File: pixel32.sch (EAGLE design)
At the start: 77 parts, among them CON1 B7B-PH-K-S-SIDE, CON10 PINHEAD_1X01-2.54, CON11 PINHEAD_1X01-2.54, CON12 PINHEAD_1X02-2.54, CON13 PINHEAD_1X07-2, CON14 PINHEAD_1X07-2, CON2 B7B-PH-K-S-SIDE, CON3 PINHEAD_1X02-2.54, CON4 PINHEAD_1X01-2.54, CON5 PINHEAD_1X01-2.54, CON6 PINHEAD_1X01-2.54, CON7 PINHEAD_1X01-2.54, CON8 PINHEAD_1X01-2.54, CON9 PINHEAD_1X01-2.54, IC1 STM32F030K6TX-LQFP32(7X7), IC3 ST3485SOIC8, IC6 MC74VHC1GT125, IC7 MC74VHC1GT125, IC8 LM317, Y1 16MHz

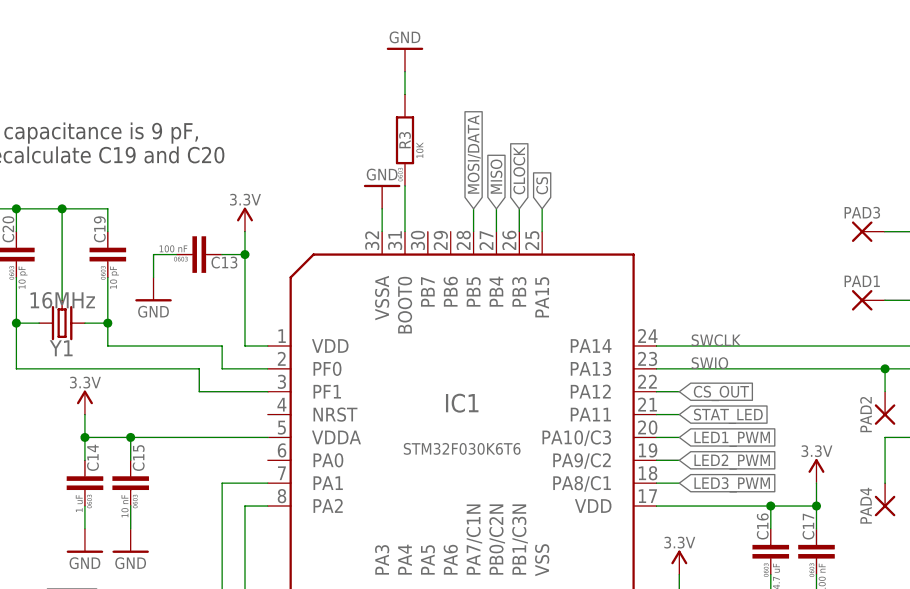
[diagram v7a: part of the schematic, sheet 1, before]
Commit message: added reset pad
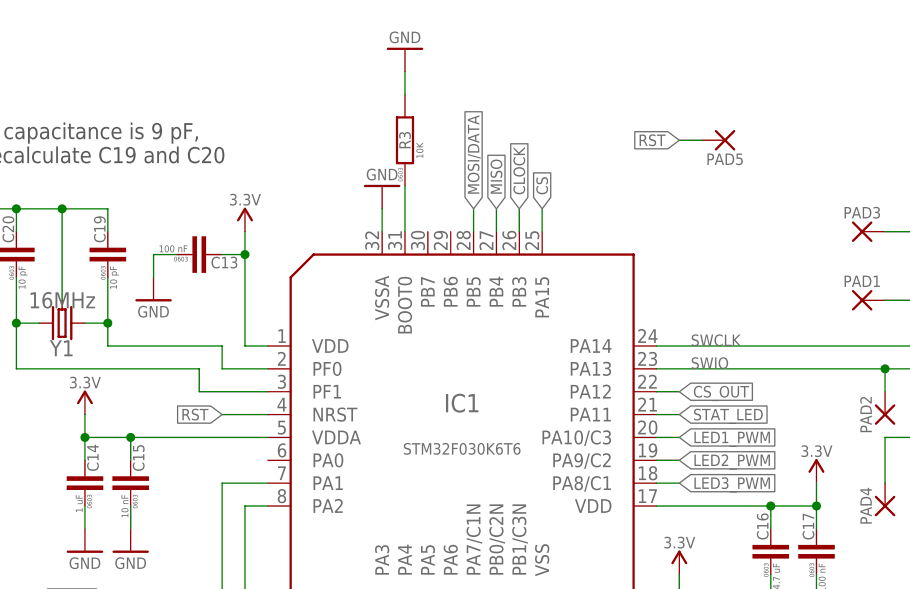
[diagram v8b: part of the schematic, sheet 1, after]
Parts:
- added PAD5: WIREPADSMD2.5-1.8, wirepad:WIREPADSMD2.5-1.8
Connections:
- new net RST: IC1.NRST, PAD5.P
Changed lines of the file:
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@@
 <grid distance="0.1" unitdist="inch" unit="inch" style="lines" multiple="1" display="no" altdistance="0.01" altunitdist="inch" altunit="inch"/>
 <layers>
-<layer number="1" name="Top" color="4" fill="1" visible="yes" active="no"/>
-<layer number="2" name="Route2" color="1" fill="3" visible="yes" active="no"/>
-<layer number="3" name="Route3" color="4" fill="3" visible="yes" active="no"/>
-<layer number="4" name="Route4" color="1" fill="4" visible="yes" active="no"/>
-<layer number="5" name="Route5" color="4" fill="4" visible="yes" active="no"/>
-<layer number="6" name="Route6" color="1" fill="8" visible="yes" active="no"/>
-<layer number="7" name="Route7" color="4" fill="8" visible="yes" active="no"/>
-<layer number="8" name="Route8" color="1" fill="2" visible="yes" active="no"/>
-<layer number="9" name="Route9" color="4" fill="2" visible="yes" active="no"/>
-<layer number="10" name="Route10" color="1" fill="7" visible="yes" active="no"/>
-<layer number="11" name="Route11" color="4" fill="7" visible="yes" active="no"/>
-<layer number="12" name="Route12" color="1" fill="5" visible="yes" active="no"/>
-<layer number="13" name="Route13" color="4" fill="5" visible="yes" active="no"/>
-<layer number="14" name="Route14" color="1" fill="6" visible="yes" active="no"/>
-<layer number="15" name="Route15" color="4" fill="6" visible="yes" active="no"/>
-<layer number="16" name="Bottom" color="1" fill="1" visible="yes" active="no"/>
-<layer number="17" name="Pads" color="2" fill="1" visible="yes" active="no"/>
-<layer number="18" name="Vias" color="2" fill="1" visible="yes" active="no"/>
-<layer number="19" name="Unrouted" color="6" fill="1" visible="yes" active="no"/>
-<layer number="20" name="Dimension" color="15" fill="1" visible="yes" active="no"/>
-<layer number="21" name="tPlace" color="7" fill="1" visible="yes" active="no"/>
-<layer number="22" name="bPlace" color="7" fill="1" visible="yes" active="no"/>
-<layer number="23" name="tOrigins" color="15" fill="1" visible="yes" active="no"/>
-<layer number="24" name="bOrigins" color="15" fill="1" visible="yes" active="no"/>
-<layer number="25" name="tNames" color="7" fill="1" visible="yes" active="no"/>
-<layer number="26" name="bNames" color="7" fill="1" visible="yes" active="no"/>
-<layer number="27" name="tValues" color="7" fill="1" visible="yes" active="no"/>
-<layer number="28" name="bValues" color="7" fill="1" visible="yes" active="no"/>
+<layer number="1" name="Top" color="4" fill="1" visible="no" active="no"/>
+<layer number="2" name="Route2" color="1" fill="3" visible="no" active="no"/>
+<layer number="3" name="Route3" color="4" fill="3" visible="no" active="no"/>
+<layer number="4" name="Route4" color="1" fill="4" visible="no" active="no"/>
+<layer number="5" name="Route5" color="4" fill="4" visible="no" active="no"/>
+<layer number="6" name="Route6" color="1" fill="8" visible="no" active="no"/>
+<layer number="7" name="Route7" color="4" fill="8" visible="no" active="no"/>
+<layer number="8" name="Route8" color="1" fill="2" visible="no" active="no"/>
+<layer number="9" name="Route9" color="4" fill="2" visible="no" active="no"/>
+<layer number="10" name="Route10" color="1" fill="7" visible="no" active="no"/>
+<layer number="11" name="Route11" color="4" fill="7" visible="no" active="no"/>
+<layer number="12" name="Route12" color="1" fill="5" visible="no" active="no"/>
+<layer number="13" name="Route13" color="4" fill="5" visible="no" active="no"/>
+<layer number="14" name="Route14" color="1" fill="6" visible="no" active="no"/>
+<layer number="15" name="Route15" color="4" fill="6" visible="no" active="no"/>
+<layer number="16" name="Bottom" color="1" fill="1" visible="no" active="no"/>
+<layer number="17" name="Pads" color="2" fill="1" visible="no" active="no"/>
+<layer number="18" name="Vias" color="2" fill="1" visible="no" active="no"/>
+<layer number="19" name="Unrouted" color="6" fill="1" visible="no" active="no"/>
+<layer number="20" name="Dimension" color="15" fill="1" visible="no" active="no"/>
+<layer number="21" name="tPlace" color="7" fill="1" visible="no" active="no"/>
+<layer number="22" name="bPlace" color="7" fill="1" visible="no" active="no"/>
+<layer number="23" name="tOrigins" color="15" fill="1" visible="no" active="no"/>
+<layer number="24" name="bOrigins" color="15" fill="1" visible="no" active="no"/>
+<layer number="25" name="tNames" color="7" fill="1" visible="no" active="no"/>
+<layer number="26" name="bNames" color="7" fill="1" visible="no" active="no"/>
+<layer number="27" name="tValues" color="7" fill="1" visible="no" active="no"/>
+<layer number="28" name="bValues" color="7" fill="1" visible="no" active="no"/>
 <layer number="29" name="tStop" color="7" fill="6" visible="no" active="no"/>
 <layer number="30" name="bStop" color="7" fill="3" visible="no" active="no"/>
@@
 <layer number="35" name="tGlue" color="7" fill="4" visible="no" active="no"/>
 <layer number="36" name="bGlue" color="7" fill="5" visible="no" active="no"/>
-<layer number="37" name="tTest" color="7" fill="1" visible="yes" active="no"/>
-<layer number="38" name="bTest" color="7" fill="1" visible="yes" active="no"/>
+<layer number="37" name="tTest" color="7" fill="1" visible="no" active="no"/>
+<layer number="38" name="bTest" color="7" fill="1" visible="no" active="no"/>
 <layer number="39" name="tKeepout" color="4" fill="11" visible="no" active="no"/>
 <layer number="40" name="bKeepout" color="1" fill="11" visible="no" active="no"/>
@@
 <layer number="44" name="Drills" color="7" fill="1" visible="no" active="no"/>
 <layer number="45" name="Holes" color="7" fill="1" visible="no" active="no"/>
-<layer number="46" name="Milling" color="3" fill="1" visible="yes" active="no"/>
-<layer number="47" name="Measures" color="7" fill="1" visible="yes" active="no"/>
-<layer number="48" name="Document" color="7" fill="1" visible="yes" active="no"/>
-<layer number="49" name="Reference" color="7" fill="1" visible="yes" active="no"/>
-<layer number="50" name="dxf" color="7" fill="1" visible="yes" active="no"/>
-<layer number="51" name="tDocu" color="7" fill="1" visible="yes" active="no"/>
-<layer number="52" name="bDocu" color="7" fill="1" visible="yes" active="no"/>
-<layer number="53" name="tGND_GNDA" color="7" fill="9" visible="yes" active="no"/>
-<layer number="54" name="bGND_GNDA" color="1" fill="9" visible="yes" active="no"/>
-<layer number="56" name="wert" color="7" fill="1" visible="yes" active="no"/>
-<layer number="57" name="tCAD" color="12" fill="1" visible="yes" active="no"/>
-<layer number="58" name="bCAD" color="9" fill="1" visible="yes" active="no"/>
-<layer number="59" name="Invisible" color="7" fill="1" visible="yes" active="no"/>
-<layer number="61" name="stand" color="7" fill="1" visible="yes" active="no"/>
+<layer number="46" name="Milling" color="3" fill="1" visible="no" active="no"/>
+<layer number="47" name="Measures" color="7" fill="1" visible="no" active="no"/>
+<layer number="48" name="Document" color="7" fill="1" visible="no" active="no"/>
+<layer number="49" name="Reference" color="7" fill="1" visible="no" active="no"/>
+<layer number="50" name="dxf" color="7" fill="1" visible="no" active="no"/>
+<layer number="51" name="tDocu" color="7" fill="1" visible="no" active="no"/>
+<layer number="52" name="bDocu" color="7" fill="1" visible="no" active="no"/>
+<layer number="53" name="tGND_GNDA" color="7" fill="9" visible="no" active="no"/>
+<layer number="54" name="bGND_GNDA" color="1" fill="9" visible="no" active="no"/>
+<layer number="56" name="wert" color="7" fill="1" visible="no" active="no"/>
+<layer number="57" name="tCAD" color="12" fill="1" visible="no" active="no"/>
+<layer number="58" name="bCAD" color="9" fill="1" visible="no" active="no"/>
+<layer number="59" name="Invisible" color="7" fill="1" visible="no" active="no"/>
+<layer number="61" name="stand" color="7" fill="1" visible="no" active="no"/>
 <layer number="90" name="Modules" color="5" fill="1" visible="yes" active="yes"/>
 <layer number="91" name="Nets" color="2" fill="1" visible="yes" active="yes"/>
@@
 </part>
 <part name="GND15" library="supply_symbols" deviceset="GND" device="" value="GND"/>
+<part name="PAD5" library="wirepad" deviceset="WIREPAD" device="SMD2.5-1.8">
+<attribute name="BOM" value="EXCLUDE"/>
+</part>
 </parts>
 <sheets>
@@
 </instance>
 <instance part="GND15" gate="1" x="78.74" y="248.92" rot="MR180"/>
+<instance part="PAD5" gate="G$1" x="114.3" y="238.76" rot="R180">
+<attribute name="BOM" x="114.3" y="238.76" size="1.778" layer="96" rot="R180" display="off"/>
+</instance>
 </instances>
 <busses>
@@
 </segment>
 </net>
+<net name="RST" class="0">
+<segment>
+<pinref part="IC1" gate="IC" pin="NRST"/>
+<wire x1="63.5" y1="208.28" x2="58.42" y2="208.28" width="0.1524" layer="91"/>
+<label x="58.42" y="208.28" size="1.27" layer="95" rot="R180" xref="yes"/>
+</segment>
+<segment>
+<pinref part="PAD5" gate="G$1" pin="P"/>
+<wire x1="111.76" y1="238.76" x2="109.22" y2="238.76" width="0.1524" layer="91"/>
+<label x="109.22" y="238.76" size="1.27" layer="95" rot="R180" xref="yes"/>
+</segment>
+</net>
